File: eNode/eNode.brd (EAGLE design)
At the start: 49.3 x 28.8 mm, 33 parts, among them IC1 MCP1700-33, IC2 MCP73831/OT

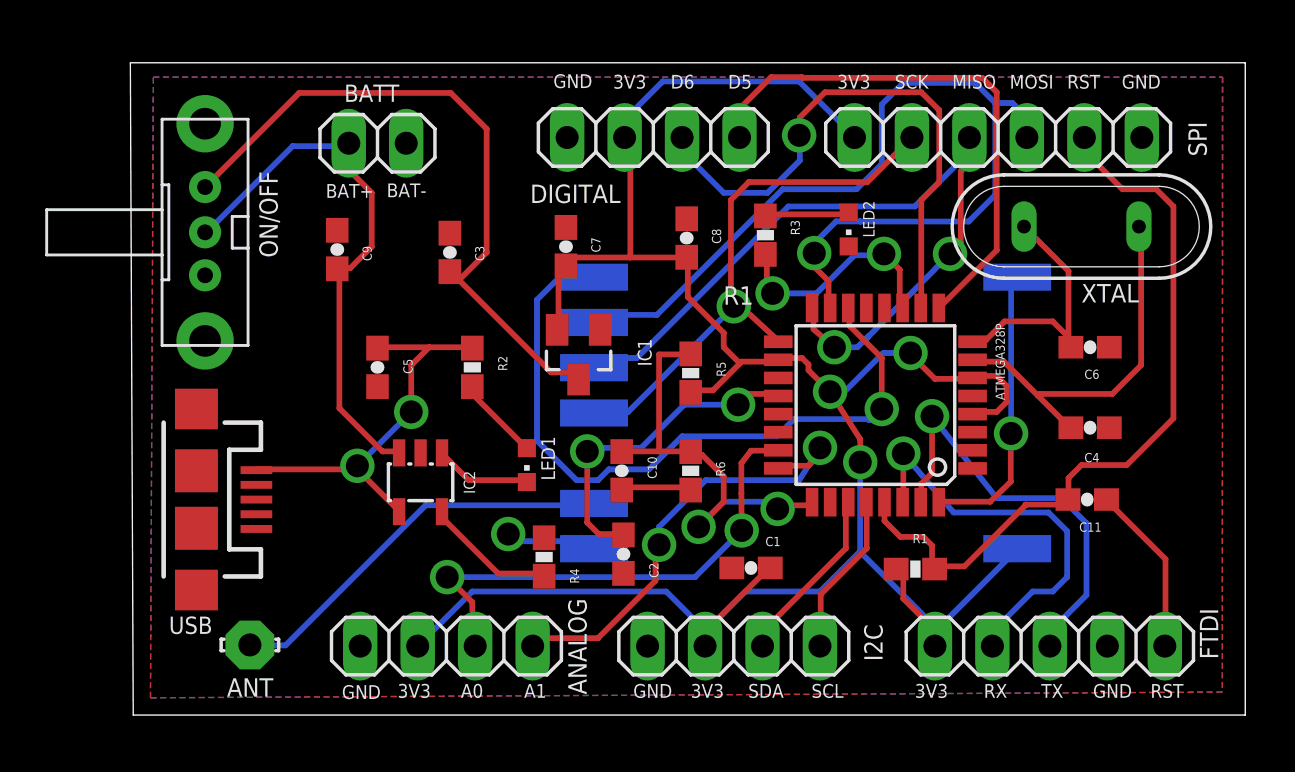
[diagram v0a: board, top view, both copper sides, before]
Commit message: Update eNode board and schematic
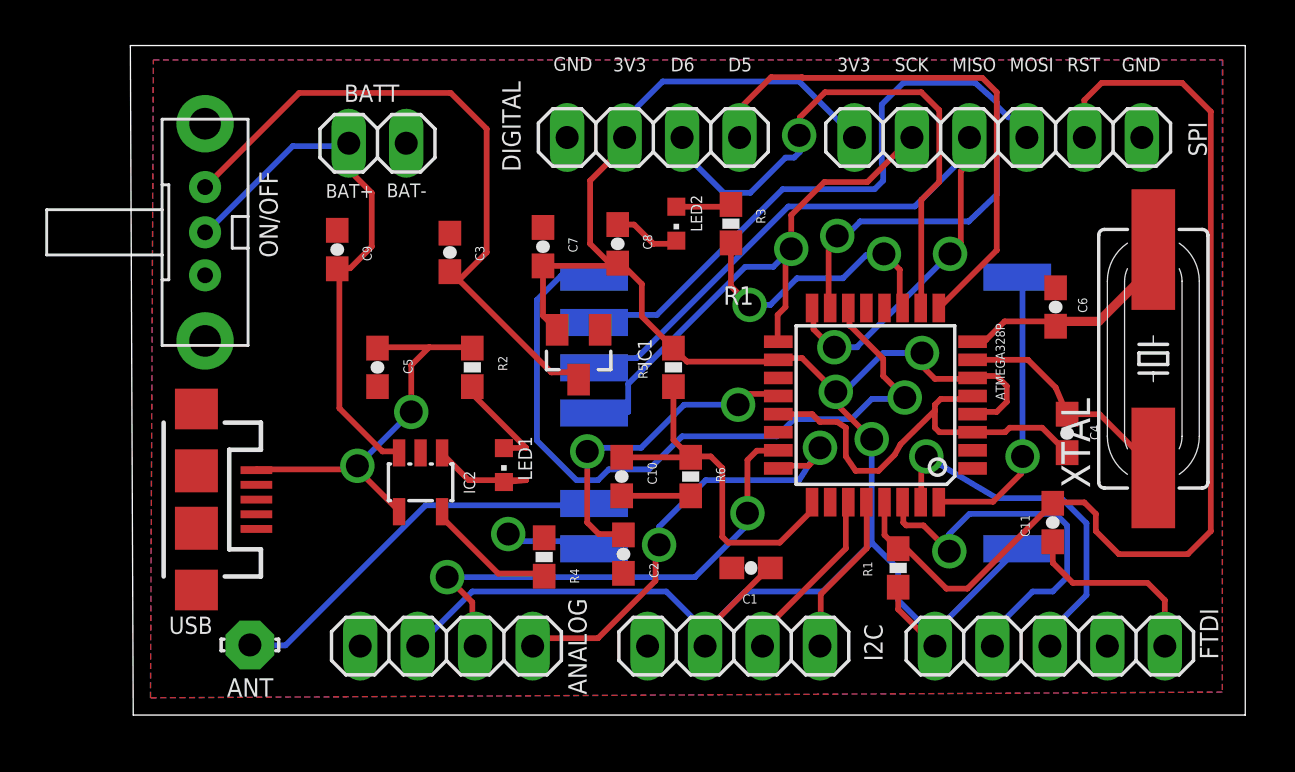
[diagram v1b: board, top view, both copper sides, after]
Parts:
- XTAL: device special:QS -> SparkFun-FreqCtrl:HC49UP
- moved LED2 7.62 mm to (45.2, 20.7)
- moved XTAL 6.65 mm to (66.3, 14.7), turned to 90 degrees
- moved C8 3.06 mm to (42.6, 19.8)
- moved C6 2.34 mm to (62.0, 17.0), turned to 90 degrees
- moved C11 1.83 mm to (61.8, 7.49), turned to 90 degrees
- moved R3 1.61 mm to (47.6, 20.7)
- moved C4 1.05 mm to (62.5, 11.4), turned to 270 degrees
- moved C7 1.02 mm to (39.3, 19.7)
- moved LED1 1.02 mm to (37.6, 10.0)
- moved R5 0.80 mm to (45.1, 14.4), turned to 90 degrees
- moved R1 0.76 mm to (55.0, 5.49), turned to 90 degrees
- moved C10 0.25 mm to (42.8, 9.53)
- moved R6 0.25 mm to (45.8, 9.53)
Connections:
- new net DTR: C11.1, FTDI.5
- net RESET: no longer C11.1, FTDI.5
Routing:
- net GND: track 4.06 -> 26.3 mm
- net DTR: track 0.00 -> 8.60 mm
- net N$3: track 16.8 -> 10.3 mm
- net RESET: track 40.9 -> 46.9 mm
- net A2: track 19.2 -> 16.2 mm, vias 2 -> 0
- net D1/TX: track 19.2 -> 16.5 mm
- net D10/SS: track 30.3 -> 32.9 mm
- net D7: track 10.3 -> 12.8 mm
- net N$8: track 3.74 -> 2.44 mm
- net N$5: track 4.39 -> 5.64 mm
- net N$4: track 11.1 -> 10.1 mm
- net N$1: track 3.73 -> 4.68 mm
- net D0/RX: track 17.9 -> 17.3 mm
- net D2: track 12.8 -> 13.3 mm
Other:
- board size 49.3 x 28.8 mm -> 49.3 x 29.6 mm
- board text removed: "A0"
- board text removed: "A1"
- board text removed: "RX"
- board text removed: "SCL"
- board text removed: "SDA"
- board text removed: "TX"

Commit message: Update final eNode version 1
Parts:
- removed C4, C6: 22pF, SparkFun-Passives:0603-CAP
- removed XTAL: (no value), SparkFun-FreqCtrl:HC49UP
- added X1: 16MHZ, SparkFun-FreqCtrl:RESONATOR-SMD
- R3: value 330 -> 1K
- moved C11 1.85 mm to (61.3, 5.71), turned to 180 degrees
- moved LED2 0.76 mm to (45.2, 19.9)
- moved R3 0.76 mm to (47.6, 19.9)
- moved IC2 0.51 mm to (33.9, 8.76)
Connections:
- net N$5 renamed STAT
- net N$7 renamed PROG
- net GND: now also X1.2; no longer C4.2, C6.2
- net N$3: now also X1.1; no longer C4.1, XTAL.1
- net N$4: now also X1.3; no longer C6.1, XTAL.2
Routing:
- net GND: track 26.3 -> 245.7 mm, vias 1 -> 2
- net N$4: track 10.1 -> 3.35 mm
- net RESET: track 46.9 -> 40.8 mm
- net N$3: track 10.3 -> 4.15 mm
- net STAT: track 5.64 -> 3.06 mm
- net VUSB: track 18.1 -> 20.3 mm
- net VBAT_RAW: track 24.5 -> 26.0 mm
- net N$1: track 4.68 -> 3.30 mm
- net DTR: track 8.60 -> 7.67 mm
- net D7: track 12.8 -> 12.0 mm
- net A0: track 21.7 -> 22.4 mm
- net VBAT: track 29.9 -> 30.5 mm
- net PROG: track 6.15 -> 5.55 mm
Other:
- board size 49.3 x 29.6 mm -> 49.3 x 30.1 mm
- board text added: "DTR"
- board text added: "RX"
- board text added: "SCL"
- board text added: "SDA"
- board text added: "TX"
